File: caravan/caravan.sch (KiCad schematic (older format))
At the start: 50 parts

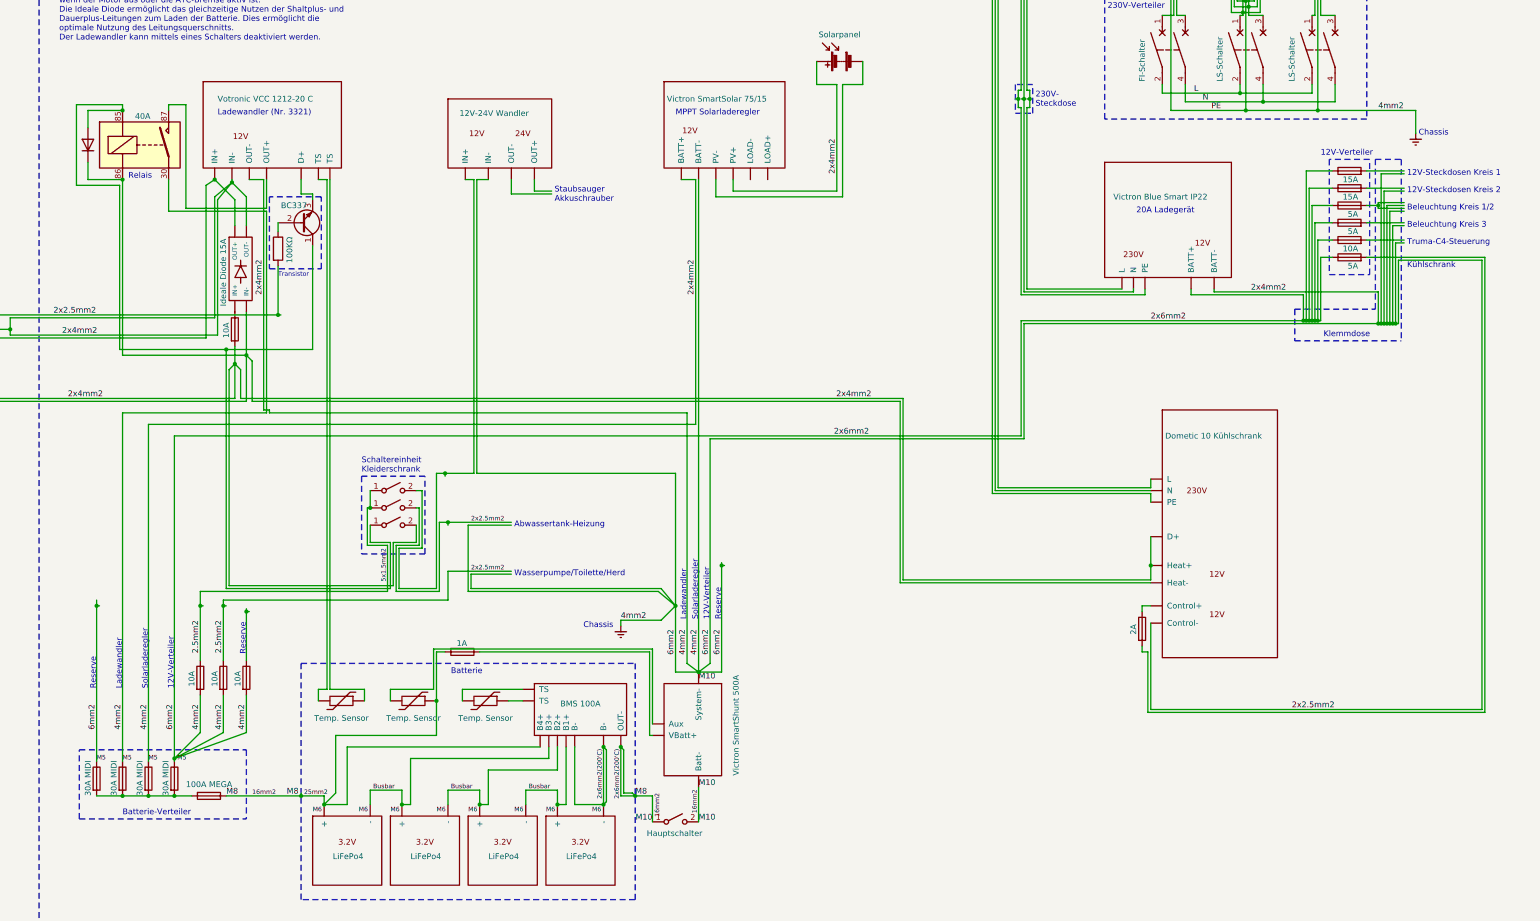
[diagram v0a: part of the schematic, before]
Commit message: caravan: Added battery distributor fuse box
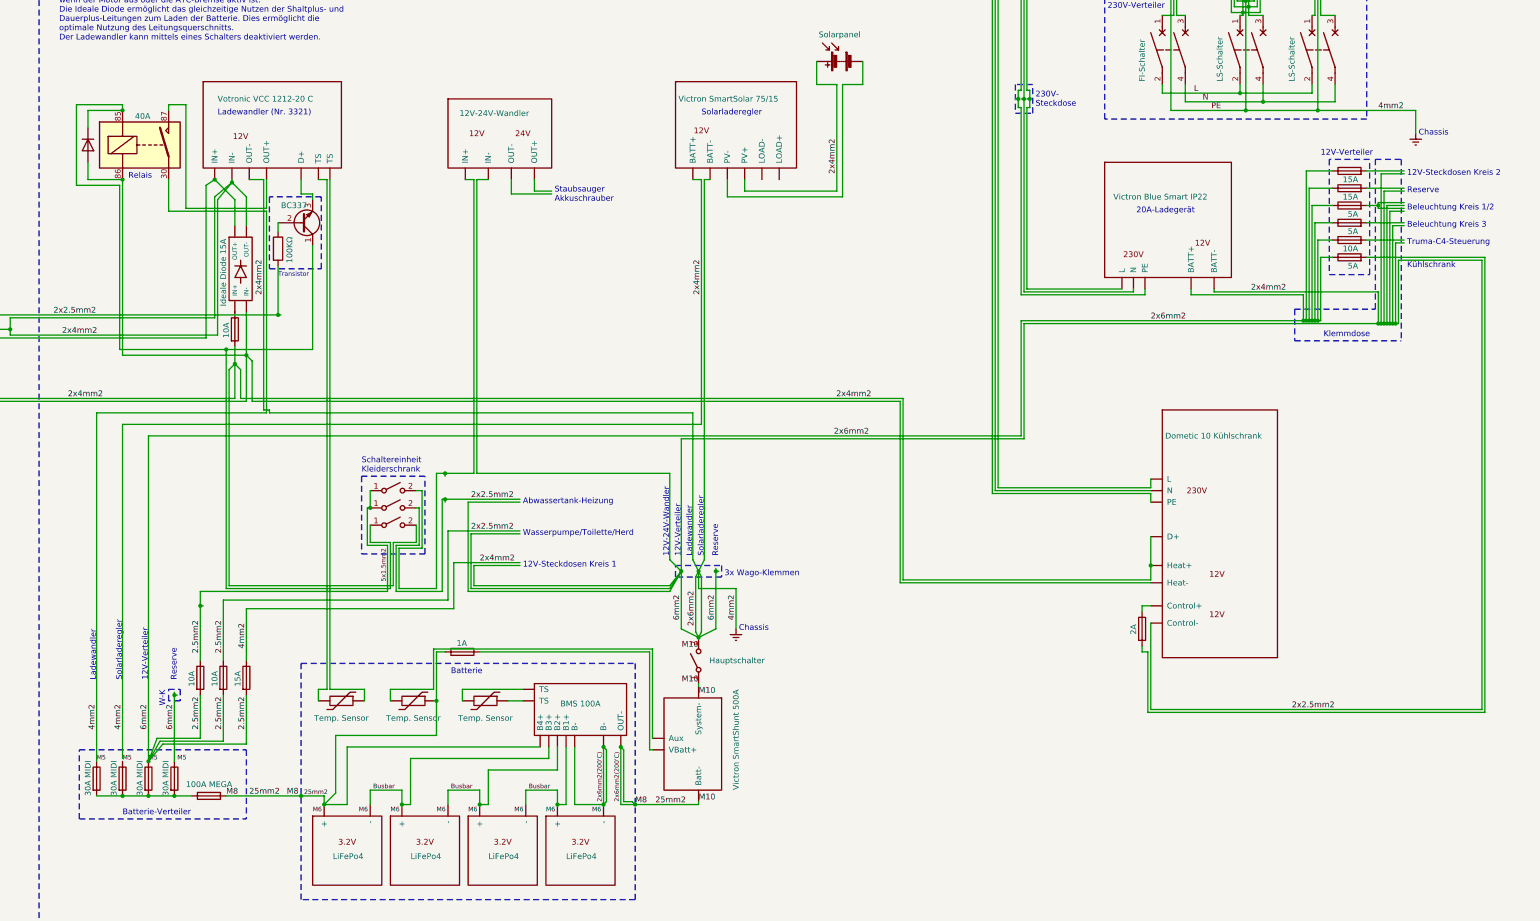
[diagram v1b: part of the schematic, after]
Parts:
- F?: value 10A -> 15A
- U?: value 12V-24V Wandler -> 12V-24V-Wandler
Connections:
- net labels removed: 16mm2
- wire segments 426 -> 439
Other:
- note added: "12V-24V-Wandler"
- note added: "20A-Ladegerät"
- note added: "3x Wago-Klemmen"
- note added: "W-K"
- note removed: "20A Ladegerät"
- note removed: "MPPT Solarladeregler"
